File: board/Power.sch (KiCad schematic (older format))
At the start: 13 parts, among them U3 L78L05_TO92

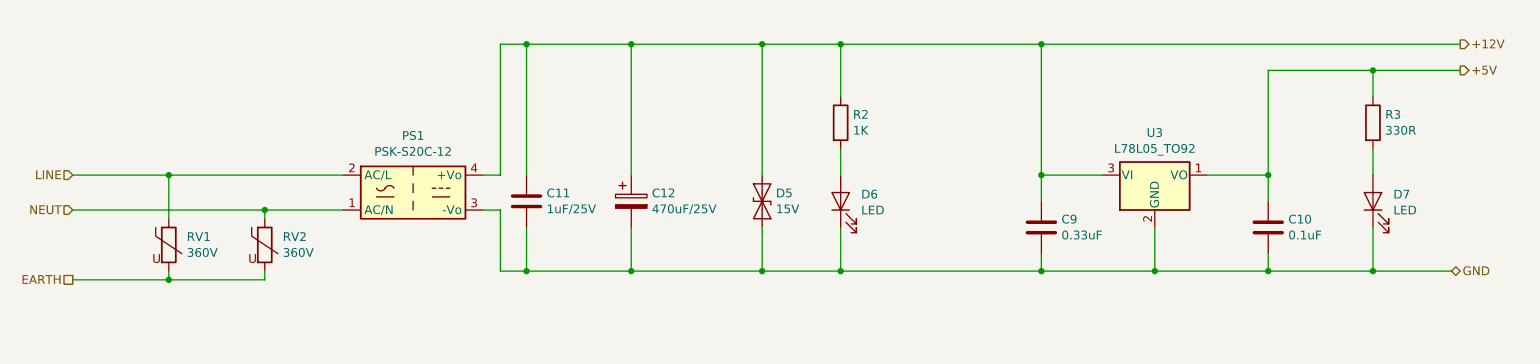
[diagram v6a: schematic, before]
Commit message: Split the 5v and 12v ground paths
* To control the return path for (noisy) relay current, split the grounds for
  the 12v and 5v sections.
* The grounds are joined by bridges (solder pads) placed adjacent to the 5v
  regulator, on both layers.
* The gound plane is split in two; conveniently the 12v vs 5v components were
  already well placed to make this straightforward.
* 12v power LED uses the 5v ground to simplify routing.
* Add dummy power flags for ERC
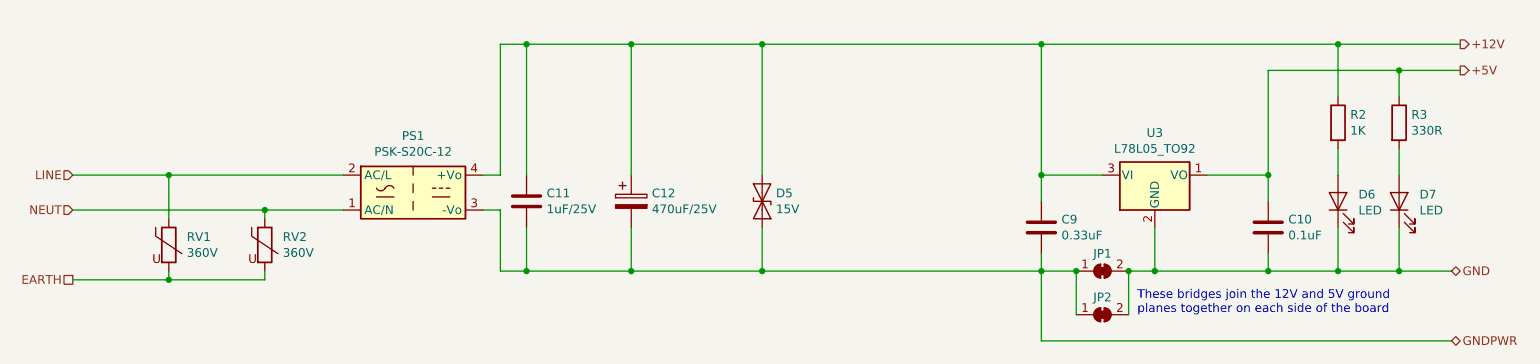
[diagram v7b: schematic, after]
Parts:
- added JP1, JP2: SolderJumper_2_Bridged, Jumper:SolderJumper-2_P1.3mm_Bridged2Bar_RoundedPad1.0x1.5mm, symbol Jumper:SolderJumper_2_Bridged
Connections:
- net GND: now also JP1.2 (B), JP2.2 (B); no longer C11.2, C12.2, C9.2, D5.2 (A2), PS1.3 (-Vo)
- new net GNDPWR: C11.2, C12.2, C9.2, D5.2 (A2), JP1.1 (A), JP2.1 (A), PS1.3 (-Vo)
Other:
- note added: "These bridges join the 12V and 5V ground\nplanes together on each side of the board"
- moved on the sheet: D6, D7, R2, R3
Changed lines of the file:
@@
 Sheet 4 4
 Title "Projector Screen Controller"
-Date "2019-09-02"
+Date "2019-09-07"
 Rev "0.2"
 Comp "Flirble Open Source"
@@
 Wire Wire Line
 	8550 3800 7900 3800
-Connection ~ 7900 3800
-Wire Wire Line
-	7900 3800 7250 3800
 Wire Wire Line
 	7250 3800 7250 3700
@@
 Connection ~ 7250 2500
 Wire Wire Line
-	7250 2500 9650 2500
+	7250 2500 8950 2500
 Text HLabel 9650 2650 2    50   Output ~ 0
 +5V
-Wire Wire Line
-	8550 2650 9150 2650
 Wire Wire Line
 	8550 2650 8550 3250
@@
 GND
 Wire Wire Line
-	8550 3800 9150 3800
+	8550 3800 8950 3800
 Connection ~ 8550 3800
-Wire Wire Line
-	7250 3800 6100 3800
-Connection ~ 7250 3800
 $Comp
 L Device:Varistor RV?
@@
 Wire Wire Line
 	5650 3250 5650 2500
-Wire Wire Line
-	5650 2500 6100 2500
 $Comp
 L Device:LED D6
 U 1 1 5D70BFF3
-P 6100 3400
-F 0 "D6" V 6139 3283 50  0000 R CNN
-F 1 "LED" V 6048 3283 50  0000 R CNN
-F 2 "LEDs:LED_D5.0mm" H 6100 3400 50  0001 C CNN
-F 3 "~" H 6100 3400 50  0001 C CNN
-	1    6100 3400
+P 8950 3400
+F 0 "D6" V 8989 3283 50  0000 R CNN
+F 1 "LED" V 8898 3283 50  0000 R CNN
+F 2 "LEDs:LED_D5.0mm" H 8950 3400 50  0001 C CNN
+F 3 "~" H 8950 3400 50  0001 C CNN
+	1    8950 3400
 	0    -1   -1   0
 $EndComp
 Wire Wire Line
-	6100 3550 6100 3800
-Connection ~ 6100 3800
-Wire Wire Line
-	6100 3800 5650 3800
+	8950 3550 8950 3800
 $Comp
 L Device:R R2
 U 1 1 5D70D964
-P 6100 2950
-F 0 "R2" H 6170 2996 50  0000 L CNN
-F 1 "1K" H 6170 2905 50  0000 L CNN
-F 2 "Resistors_THT:R_Axial_DIN0207_L6.3mm_D2.5mm_P10.16mm_Horizontal" V 6030 2950 50  0001 C CNN
-F 3 "~" H 6100 2950 50  0001 C CNN
-	1    6100 2950
-	1    0    0    -1
-$EndComp
-Wire Wire Line
-	6100 2800 6100 2500
-Connection ~ 6100 2500
-Wire Wire Line
-	6100 2500 7250 2500
-Wire Wire Line
-	6100 3100 6100 3250
+P 8950 2950
+F 0 "R2" H 9020 2996 50  0000 L CNN
+F 1 "1K" H 9020 2905 50  0000 L CNN
+F 2 "Resistors_THT:R_Axial_DIN0207_L6.3mm_D2.5mm_P10.16mm_Horizontal" V 8880 2950 50  0001 C CNN
+F 3 "~" H 8950 2950 50  0001 C CNN
+	1    8950 2950
+	1    0    0    -1
+$EndComp
+Wire Wire Line
+	8950 2800 8950 2500
+Wire Wire Line
+	8950 3100 8950 3250
 $Comp
 L Device:LED D7
 U 1 1 5D70F3A3
-P 9150 3400
-F 0 "D7" V 9189 3283 50  0000 R CNN
-F 1 "LED" V 9098 3283 50  0000 R CNN
-F 2 "LEDs:LED_D5.0mm" H 9150 3400 50  0001 C CNN
-F 3 "~" H 9150 3400 50  0001 C CNN
-	1    9150 3400
+P 9300 3400
+F 0 "D7" V 9339 3283 50  0000 R CNN
+F 1 "LED" V 9248 3283 50  0000 R CNN
+F 2 "LEDs:LED_D5.0mm" H 9300 3400 50  0001 C CNN
+F 3 "~" H 9300 3400 50  0001 C CNN
+	1    9300 3400
 	0    -1   -1   0
 $EndComp
 Wire Wire Line
-	9150 3550 9150 3800
-Connection ~ 9150 3800
-Wire Wire Line
-	9150 3800 9600 3800
+	9300 3550 9300 3800
 $Comp
 L Device:R R3
 U 1 1 5D710E5B
-P 9150 2950
-F 0 "R3" H 9220 2996 50  0000 L CNN
-F 1 "330R" H 9220 2905 50  0000 L CNN
-F 2 "Resistors_THT:R_Axial_DIN0207_L6.3mm_D2.5mm_P10.16mm_Horizontal" V 9080 2950 50  0001 C CNN
-F 3 "~" H 9150 2950 50  0001 C CNN
-	1    9150 2950
-	1    0    0    -1
-$EndComp
-Wire Wire Line
-	9150 3100 9150 3250
-Wire Wire Line
-	9150 2800 9150 2650
-Connection ~ 9150 2650
-Wire Wire Line
-	9150 2650 9650 2650
+P 9300 2950
+F 0 "R3" H 9370 2996 50  0000 L CNN
+F 1 "330R" H 9370 2905 50  0000 L CNN
+F 2 "Resistors_THT:R_Axial_DIN0207_L6.3mm_D2.5mm_P10.16mm_Horizontal" V 9230 2950 50  0001 C CNN
+F 3 "~" H 9300 2950 50  0001 C CNN
+	1    9300 2950
+	1    0    0    -1
+$EndComp
+Wire Wire Line
+	9300 3100 9300 3250
+Wire Wire Line
+	9300 2800 9300 2650
 Wire Wire Line
 	4150 3800 4300 3800
@@
 Wire Wire Line
 	4300 2500 4900 2500
+$Comp
+L Jumper:SolderJumper_2_Bridged JP?
+U 1 1 5D7501DC
+P 7600 3800
+AR Path="/5D7501DC" Ref="JP?"  Part="1"
+AR Path="/5D68B9FF/5D7501DC" Ref="JP1"  Part="1"
+F 0 "JP1" H 7600 3900 50  0000 C CNN
+F 1 "SolderJumper_2_Bridged" H 7900 3700 50  0001 C CNN
+F 2 "Jumper:SolderJumper-2_P1.3mm_Bridged2Bar_RoundedPad1.0x1.5mm" H 7600 3800 50  0001 C CNN
+F 3 "~" H 7600 3800 50  0001 C CNN
+	1    7600 3800
+	1    0    0    -1
+$EndComp
+Wire Wire Line
+	7750 3800 7900 3800
+Connection ~ 7900 3800
+Wire Wire Line
+	7450 3800 7250 3800
+Connection ~ 7250 3800
+Text HLabel 9600 4200 2    50   BiDi ~ 0
+GNDPWR
+Wire Wire Line
+	7250 4200 9600 4200
+Connection ~ 8950 2500
+Wire Wire Line
+	8950 2500 9650 2500
+Connection ~ 8950 3800
+Wire Wire Line
+	5650 3800 7250 3800
+Wire Wire Line
+	5650 2500 7250 2500
+Connection ~ 9300 2650
+Wire Wire Line
+	9300 2650 9650 2650
+Connection ~ 9300 3800
+Wire Wire Line
+	9300 3800 9600 3800
+Wire Wire Line
+	8550 2650 9300 2650
+Wire Wire Line
+	8950 3800 9300 3800
+Wire Wire Line
+	7250 4200 7250 3800
+$Comp
+L Jumper:SolderJumper_2_Bridged JP?
+U 1 1 5D77C086
+P 7600 4050
+AR Path="/5D77C086" Ref="JP?"  Part="1"
+AR Path="/5D68B9FF/5D77C086" Ref="JP2"  Part="1"
+F 0 "JP2" H 7600 4150 50  0000 C CNN
+F 1 "SolderJumper_2_Bridged" H 7900 3950 50  0001 C CNN
+F 2 "Jumper:SolderJumper-2_P1.3mm_Bridged2Bar_RoundedPad1.0x1.5mm" H 7600 4050 50  0001 C CNN
+F 3 "~" H 7600 4050 50  0001 C CNN
+	1    7600 4050
+	1    0    0    -1
+$EndComp
+Wire Wire Line
+	7450 4050 7450 3800
+Connection ~ 7450 3800
+Wire Wire Line
+	7750 4050 7750 3800
+Connection ~ 7750 3800
+Text Notes 7800 4050 0    50   ~ 0
+These bridges join the 12V and 5V ground\nplanes together on each side of the board
 $EndSCHEMATC

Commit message: Update all footprints to KiCad 5 paths
* All footprints updated.
* 3D models for the relays seem to be missing from KiCad, however, so I
  have a copy in my personal library. Mostly cosmetic.
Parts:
- C10, C11, C9: footprint Capacitors_THT:C_Disc_D5.0mm_W2.5mm_P2.50mm -> Capacitor_THT:C_Disc_D5.0mm_W2.5mm_P2.50mm
- C12: footprint Capacitors_THT:CP_Radial_D10.0mm_P2.50mm_P5.00mm -> Capacitor_THT:CP_Radial_D10.0mm_P2.50mm_P5.00mm
- D5: footprint Diodes_THT:D_DO-41_SOD81_P10.16mm_Horizontal -> Diode_THT:D_DO-41_SOD81_P10.16mm_Horizontal
- D6, D7: footprint LEDs:LED_D5.0mm -> LED_THT:LED_D5.0mm
- R2, R3: footprint Resistors_THT:R_Axial_DIN0207_L6.3mm_D2.5mm_P10.16mm_Horizontal -> Resistor_THT:R_Axial_DIN0207_L6.3mm_D2.5mm_P10.16mm_Horizontal
- U3: footprint TO_SOT_Packages_THT:TO-92_Molded_Narrow_Oval -> Package_TO_SOT_THT:TO-92L
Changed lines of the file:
@@
 F 0 "U3" H 7900 3492 50  0000 C CNN
 F 1 "L78L05_TO92" H 7900 3401 50  0000 C CNN
-F 2 "TO_SOT_Packages_THT:TO-92_Molded_Narrow_Oval" H 7900 3475 50  0001 C CIN
+F 2 "Package_TO_SOT_THT:TO-92L" H 7900 3475 50  0001 C CIN
 F 3 "http://www.st.com/content/ccc/resource/technical/document/datasheet/15/55/e5/aa/23/5b/43/fd/CD00000446.pdf/files/CD00000446.pdf/jcr:content/translations/en.CD00000446.pdf" H 7900 3200 50  0001 C CNN
 	1    7900 3250
@@
 F 0 "C9" H 7365 3596 50  0000 L CNN
 F 1 "0.33uF" H 7365 3505 50  0000 L CNN
-F 2 "Capacitors_THT:C_Disc_D5.0mm_W2.5mm_P2.50mm" H 7288 3400 50  0001 C CNN
+F 2 "Capacitor_THT:C_Disc_D5.0mm_W2.5mm_P2.50mm" H 7288 3400 50  0001 C CNN
 F 3 "~" H 7250 3550 50  0001 C CNN
 	1    7250 3550
@@
 F 0 "C10" H 8665 3596 50  0000 L CNN
 F 1 "0.1uF" H 8665 3505 50  0000 L CNN
-F 2 "Capacitors_THT:C_Disc_D5.0mm_W2.5mm_P2.50mm" H 8588 3400 50  0001 C CNN
+F 2 "Capacitor_THT:C_Disc_D5.0mm_W2.5mm_P2.50mm" H 8588 3400 50  0001 C CNN
 F 3 "~" H 8550 3550 50  0001 C CNN
 	1    8550 3550
@@
 F 0 "C11" H 4415 3446 50  0000 L CNN
 F 1 "1uF/25V" H 4415 3355 50  0000 L CNN
-F 2 "Capacitors_THT:C_Disc_D5.0mm_W2.5mm_P2.50mm" H 4338 3250 50  0001 C CNN
+F 2 "Capacitor_THT:C_Disc_D5.0mm_W2.5mm_P2.50mm" H 4338 3250 50  0001 C CNN
 F 3 "~" H 4300 3400 50  0001 C CNN
 	1    4300 3400
@@
 F 0 "C12" H 5018 3446 50  0000 L CNN
 F 1 "470uF/25V" H 5018 3355 50  0000 L CNN
-F 2 "Capacitors_THT:CP_Radial_D10.0mm_P2.50mm_P5.00mm" H 4938 3250 50  0001 C CNN
+F 2 "Capacitor_THT:CP_Radial_D10.0mm_P2.50mm_P5.00mm" H 4938 3250 50  0001 C CNN
 F 3 "~" H 4900 3400 50  0001 C CNN
 	1    4900 3400
@@
 F 0 "D5" V 5604 3479 50  0000 L CNN
 F 1 "15V" V 5695 3479 50  0000 L CNN
-F 2 "Diodes_THT:D_DO-41_SOD81_P10.16mm_Horizontal" H 5650 3400 50  0001 C CNN
+F 2 "Diode_THT:D_DO-41_SOD81_P10.16mm_Horizontal" H 5650 3400 50  0001 C CNN
 F 3 "https://www.mouser.com/datasheet/2/427/15ke-240293.pdf" H 5650 3400 50  0001 C CNN
 F 4 "Vishay" H 5650 3400 50  0001 C CNN "mfr"
@@
 F 0 "D6" V 8989 3283 50  0000 R CNN
 F 1 "LED" V 8898 3283 50  0000 R CNN
-F 2 "LEDs:LED_D5.0mm" H 8950 3400 50  0001 C CNN
+F 2 "LED_THT:LED_D5.0mm" H 8950 3400 50  0001 C CNN
 F 3 "~" H 8950 3400 50  0001 C CNN
 	1    8950 3400
@@
 F 0 "R2" H 9020 2996 50  0000 L CNN
 F 1 "1K" H 9020 2905 50  0000 L CNN
-F 2 "Resistors_THT:R_Axial_DIN0207_L6.3mm_D2.5mm_P10.16mm_Horizontal" V 8880 2950 50  0001 C CNN
+F 2 "Resistor_THT:R_Axial_DIN0207_L6.3mm_D2.5mm_P10.16mm_Horizontal" V 8880 2950 50  0001 C CNN
 F 3 "~" H 8950 2950 50  0001 C CNN
 	1    8950 2950
@@
 F 0 "D7" V 9339 3283 50  0000 R CNN
 F 1 "LED" V 9248 3283 50  0000 R CNN
-F 2 "LEDs:LED_D5.0mm" H 9300 3400 50  0001 C CNN
+F 2 "LED_THT:LED_D5.0mm" H 9300 3400 50  0001 C CNN
 F 3 "~" H 9300 3400 50  0001 C CNN
 	1    9300 3400
@@
 F 0 "R3" H 9370 2996 50  0000 L CNN
 F 1 "330R" H 9370 2905 50  0000 L CNN
-F 2 "Resistors_THT:R_Axial_DIN0207_L6.3mm_D2.5mm_P10.16mm_Horizontal" V 9230 2950 50  0001 C CNN
+F 2 "Resistor_THT:R_Axial_DIN0207_L6.3mm_D2.5mm_P10.16mm_Horizontal" V 9230 2950 50  0001 C CNN
 F 3 "~" H 9300 2950 50  0001 C CNN
 	1    9300 2950
